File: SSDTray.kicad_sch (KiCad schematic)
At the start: 22 parts, among them J1 SSD1, J10 SSD10, J11 SSD11, J12 SSD12, J13 SSD13, J14 SSD14, J15 SSD15, J16 SSD16, J17 SSD17, J18 SSD18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

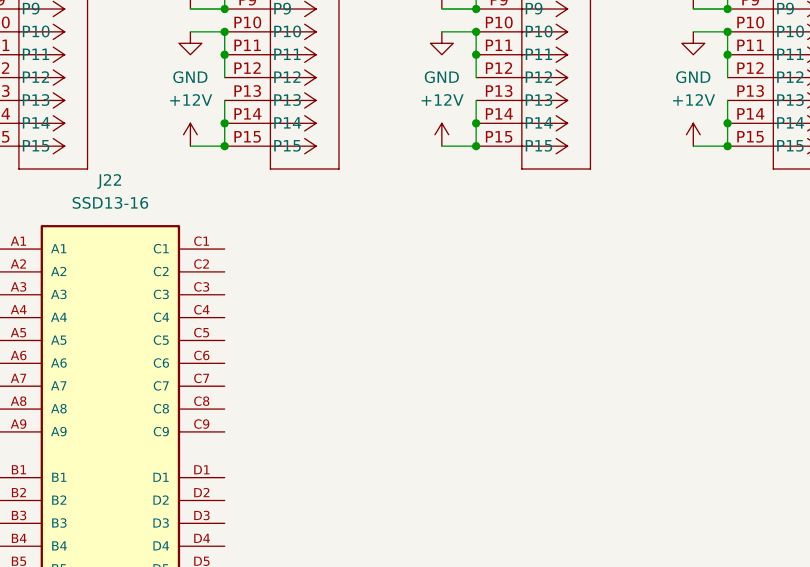
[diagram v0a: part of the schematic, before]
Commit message: Add Molex Connector footprint and symbol to libraries
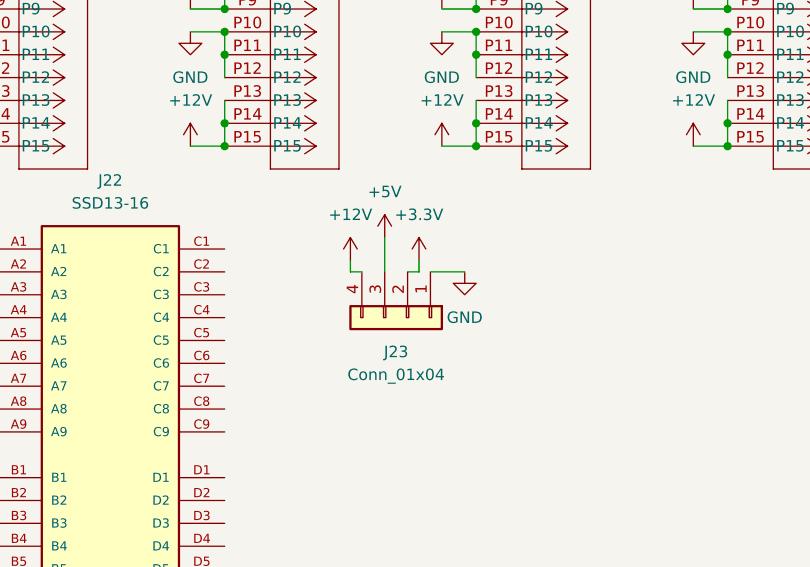
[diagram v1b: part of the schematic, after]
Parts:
- added J23: Conn_01x04, Connector_PinHeader_2.54mm:PinHeader_1x04_P2.54mm_Vertical, symbol Connector_Generic:Conn_01x04
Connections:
- net +12V: now also J23.4 (Pin_4)
- net +3.3V: now also J23.2 (Pin_2)
- net +5V: now also J23.3 (Pin_3)
- net GND: now also J23.1 (Pin_1)

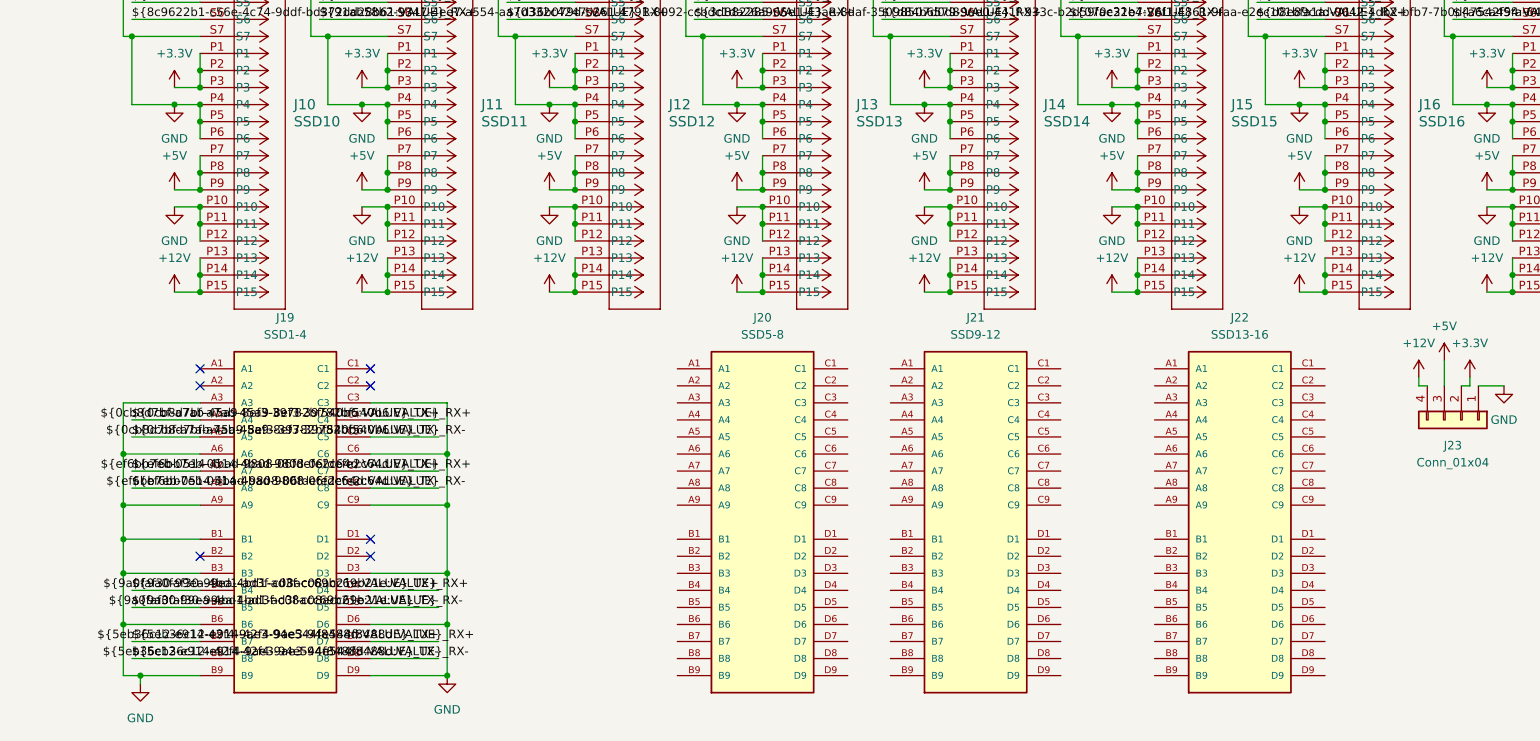
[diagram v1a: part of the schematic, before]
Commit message: Add Mini SAS footprint and symbol to libraries; update design rules and dimensions in SSDTray.kicad_pro
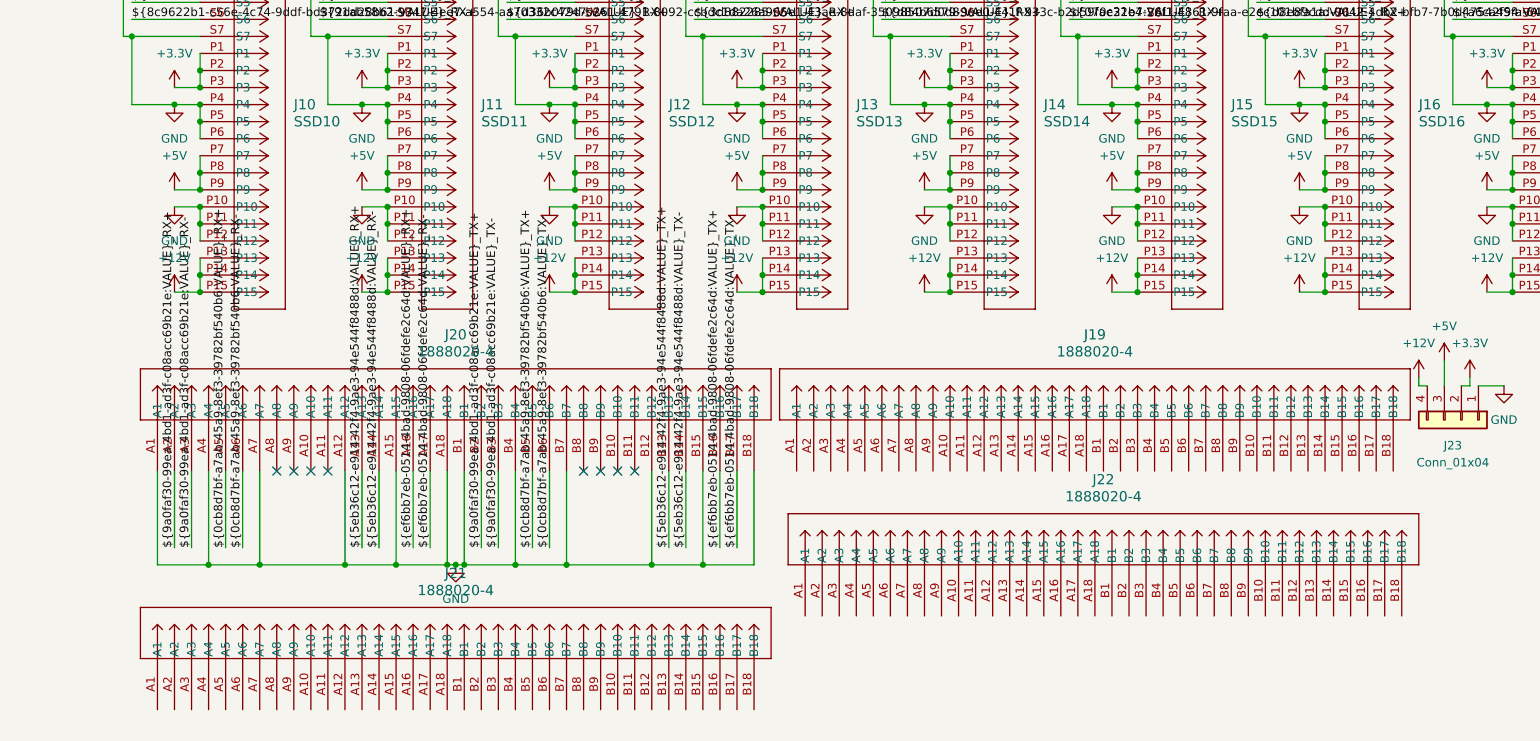
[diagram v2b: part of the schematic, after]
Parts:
- removed J19: SSD1-4, Mini SAS HD:TE_2227595-1, symbol MiniSAS HD:2227595-1
- removed J20: SSD5-8, Mini SAS HD:TE_2227595-1, symbol MiniSAS HD:2227595-1
- removed J21: SSD9-12, Mini SAS HD:TE_2227595-1, symbol MiniSAS HD:2227595-1
- removed J22: SSD13-16, Mini SAS HD:TE_2227595-1, symbol MiniSAS HD:2227595-1
- added J19, J20, J21, J22: 1888020-4, Mini SAS:CONN36_1888020-4_TEC, symbol Mini-SAS:1888020-4
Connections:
- net ${0cb8d7bf-a7ab-45a9-8ef3-39782bf540b6:VALUE}_RX+: now also J20.A5
- net ${0cb8d7bf-a7ab-45a9-8ef3-39782bf540b6:VALUE}_RX-: now also J20.A6
- net ${0cb8d7bf-a7ab-45a9-8ef3-39782bf540b6:VALUE}_TX+: now also J20.B5
- net ${0cb8d7bf-a7ab-45a9-8ef3-39782bf540b6:VALUE}_TX-: now also J20.B6
- net ${5eb36c12-e914-42f4-9ae3-94e544f8488d:VALUE}_RX+: now also J20.A13
- net ${5eb36c12-e914-42f4-9ae3-94e544f8488d:VALUE}_RX-: now also J20.A14
- net ${5eb36c12-e914-42f4-9ae3-94e544f8488d:VALUE}_TX+: now also J20.B13
- net ${5eb36c12-e914-42f4-9ae3-94e544f8488d:VALUE}_TX-: now also J20.B14
- net ${9a0faf30-99ea-4bd1-ad3f-c08acc69b21e:VALUE}_RX+: now also J20.A2
- net ${9a0faf30-99ea-4bd1-ad3f-c08acc69b21e:VALUE}_RX-: now also J20.A3
- net ${9a0faf30-99ea-4bd1-ad3f-c08acc69b21e:VALUE}_TX+: now also J20.B2
- net ${9a0faf30-99ea-4bd1-ad3f-c08acc69b21e:VALUE}_TX-: now also J20.B3
- net ${ef6bb7eb-0514-4bad-9808-06fdefe2c64d:VALUE}_RX+: now also J20.A16
- net ${ef6bb7eb-0514-4bad-9808-06fdefe2c64d:VALUE}_RX-: now also J20.A17
- net ${ef6bb7eb-0514-4bad-9808-06fdefe2c64d:VALUE}_TX+: now also J20.B16
- net ${ef6bb7eb-0514-4bad-9808-06fdefe2c64d:VALUE}_TX-: now also J20.B17
- net GND: now also J20.A1, J20.A12, J20.A15, J20.A18, J20.A4, J20.A7, J20.B1, J20.B12, J20.B15, J20.B18, J20.B4, J20.B7
- no-connect marks 7 -> 8

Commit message: Limiting to 4 drives for testing
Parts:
- removed J10: SSD10, SSD Connector:CONN_877791001_MOL, symbol SSD Connector:877791001
- removed J11: SSD11, SSD Connector:CONN_877791001_MOL, symbol SSD Connector:877791001
- removed J12: SSD12, SSD Connector:CONN_877791001_MOL, symbol SSD Connector:877791001
- removed J13: SSD13, SSD Connector:CONN_877791001_MOL, symbol SSD Connector:877791001
- removed J14: SSD14, SSD Connector:CONN_877791001_MOL, symbol SSD Connector:877791001
- removed J15: SSD15, SSD Connector:CONN_877791001_MOL, symbol SSD Connector:877791001
- removed J16: SSD16, SSD Connector:CONN_877791001_MOL, symbol SSD Connector:877791001
- removed J17: SSD17, SSD Connector:CONN_877791001_MOL, symbol SSD Connector:877791001
- removed J18: SSD18, SSD Connector:CONN_877791001_MOL, symbol SSD Connector:877791001
- removed J19, J21, J22: 1888020-4, Mini SAS:CONN36_1888020-4_TEC, symbol Mini-SAS:1888020-4
- removed J23: Conn_01x04, Connector_PinHeader_2.54mm:PinHeader_1x04_P2.54mm_Vertical, symbol Connector_Generic:Conn_01x04
- removed J5: SSD5, SSD Connector:CONN_877791001_MOL, symbol SSD Connector:877791001
- removed J6: SSD6, SSD Connector:CONN_877791001_MOL, symbol SSD Connector:877791001
- removed J7: SSD7, SSD Connector:CONN_877791001_MOL, symbol SSD Connector:877791001
- removed J8: SSD8, SSD Connector:CONN_877791001_MOL, symbol SSD Connector:877791001
- removed J9: SSD9, SSD Connector:CONN_877791001_MOL, symbol SSD Connector:877791001
- added U1: 350211-1, 4Pin ATX Molex:350211-1_TYC, symbol Molex Connector:350211-1
- renumbered J20 to J5
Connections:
- net +12V: now also U1.1
- net +5V: now also U1.4
- net GND: now also U1.2, U1.3
- removed net +3.3V: J1.P1, J1.P2, J1.P3, J2.P1, J2.P2, J2.P3, J3.P1, J3.P2, J3.P3, J4.P1, J4.P2, J4.P3
- new net: J2.P1, J2.P2, J2.P3
- new net: J3.P1, J3.P2, J3.P3
- new net: J1.P1, J1.P2, J1.P3
- new net: J4.P1, J4.P2, J4.P3
- no-connect marks 8 -> 12
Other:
- moved on the sheet: J5
